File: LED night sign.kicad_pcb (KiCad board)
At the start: 2 copper layers, 42.9 x 36.7 mm, 38 parts, among them Q1 MOSFET-NCH-2N7002PW, Q2 BC817, U1 ATtiny85-20M, U2 APDS-9301

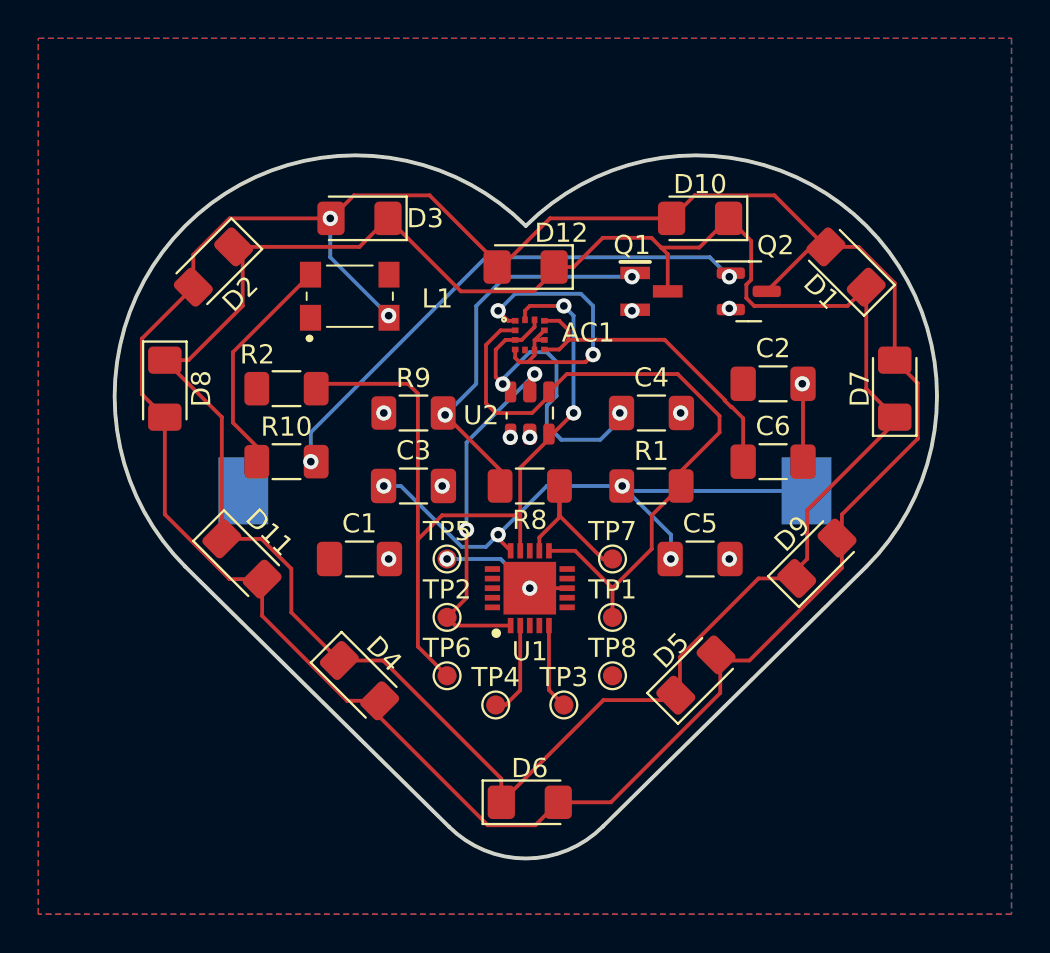
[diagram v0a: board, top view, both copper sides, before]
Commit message: Enh pcb layout
repositioned leds to be more symmetrical
improved silkscreens
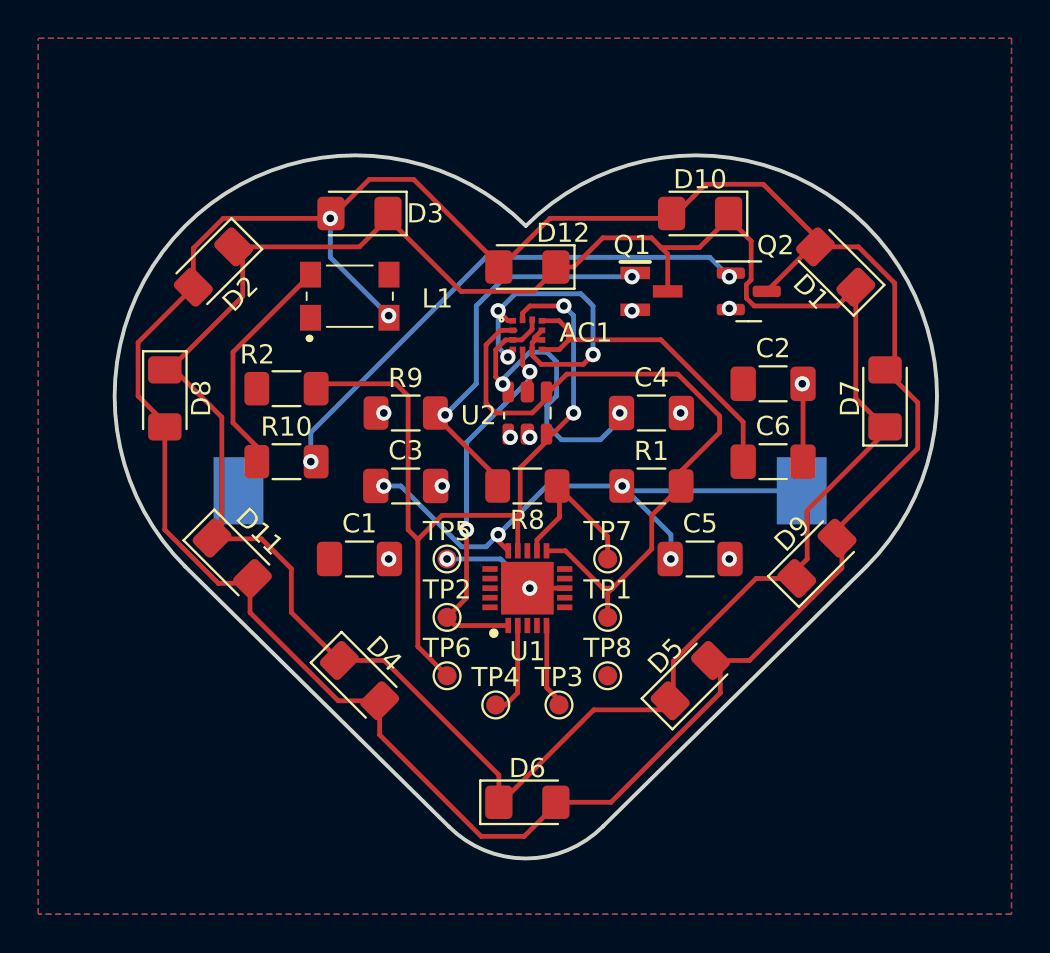
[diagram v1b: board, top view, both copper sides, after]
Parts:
- BT1: value Battery_Cell -> 2032
- moved D7 0.72 mm to (168.7, 98.6)
- moved D1 0.54 mm to (166.1, 91.7)
- moved D11 0.51 mm to (134.6, 106.9)
- moved D8 0.51 mm to (131.1, 98.6)
- moved D5 0.41 mm to (158.5, 113.3)
- moved C3 0.41 mm to (143.6, 103.1)
- moved R9 0.41 mm to (143.6, 99.3)
- moved BT1 0.25 mm to (149.6, 103.4)
- moved D10 0.25 mm to (159.0, 88.9)
- moved D3 0.25 mm to (141.2, 88.9)
- moved TP1 0.25 mm to (154.2, 110.0)
- moved TP3 0.25 mm to (151.6, 114.6)
- moved TP7 0.25 mm to (154.2, 106.9)
- moved TP8 0.25 mm to (154.2, 113.0)
- moved AC1 0.13 mm to (150.0, 95.2)
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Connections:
- AC1 pad 5: unconnected-(AC1-Pad5) -> INT
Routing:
- net JouleThiefPWR: track 135.7 -> 138.5 mm
- net INT: track 19.1 -> 20.3 mm
- net GND: track 27.5 -> 28.7 mm, vias 14 -> 15

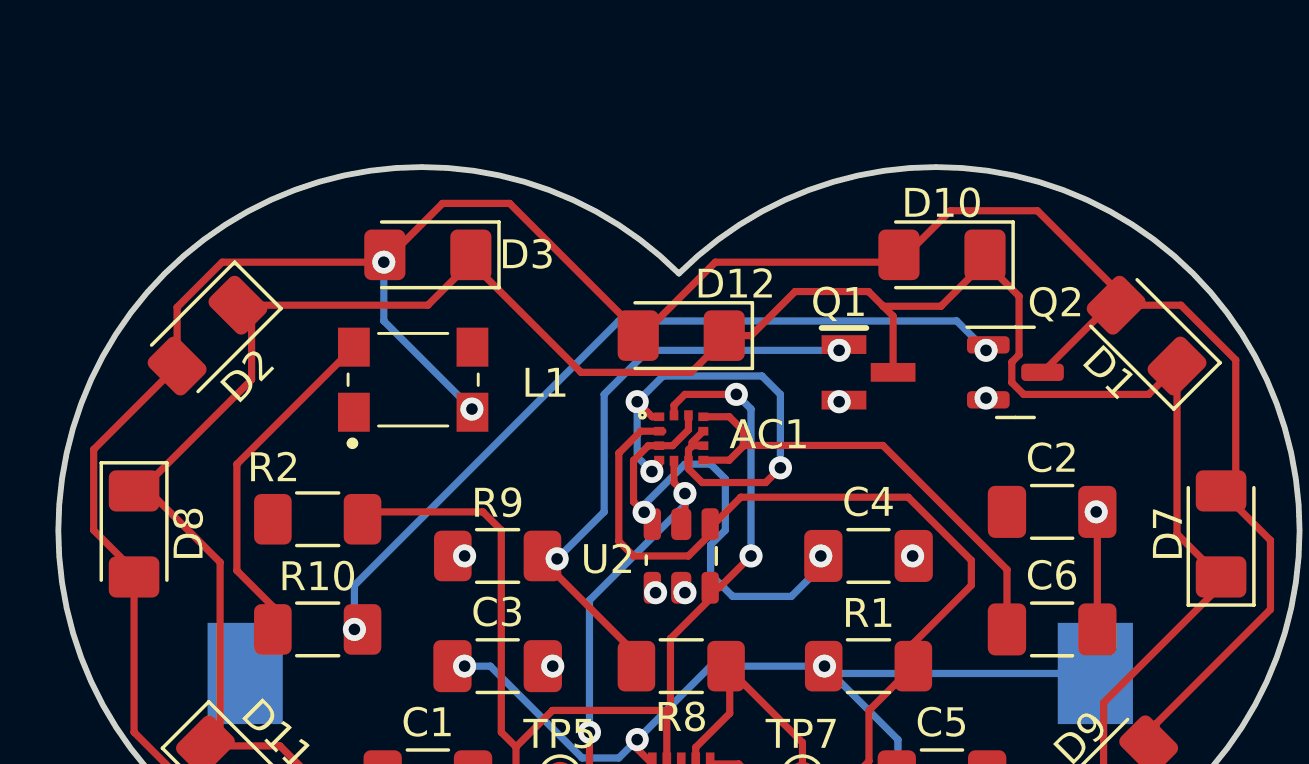
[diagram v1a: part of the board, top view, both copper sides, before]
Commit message: made room for potential holes
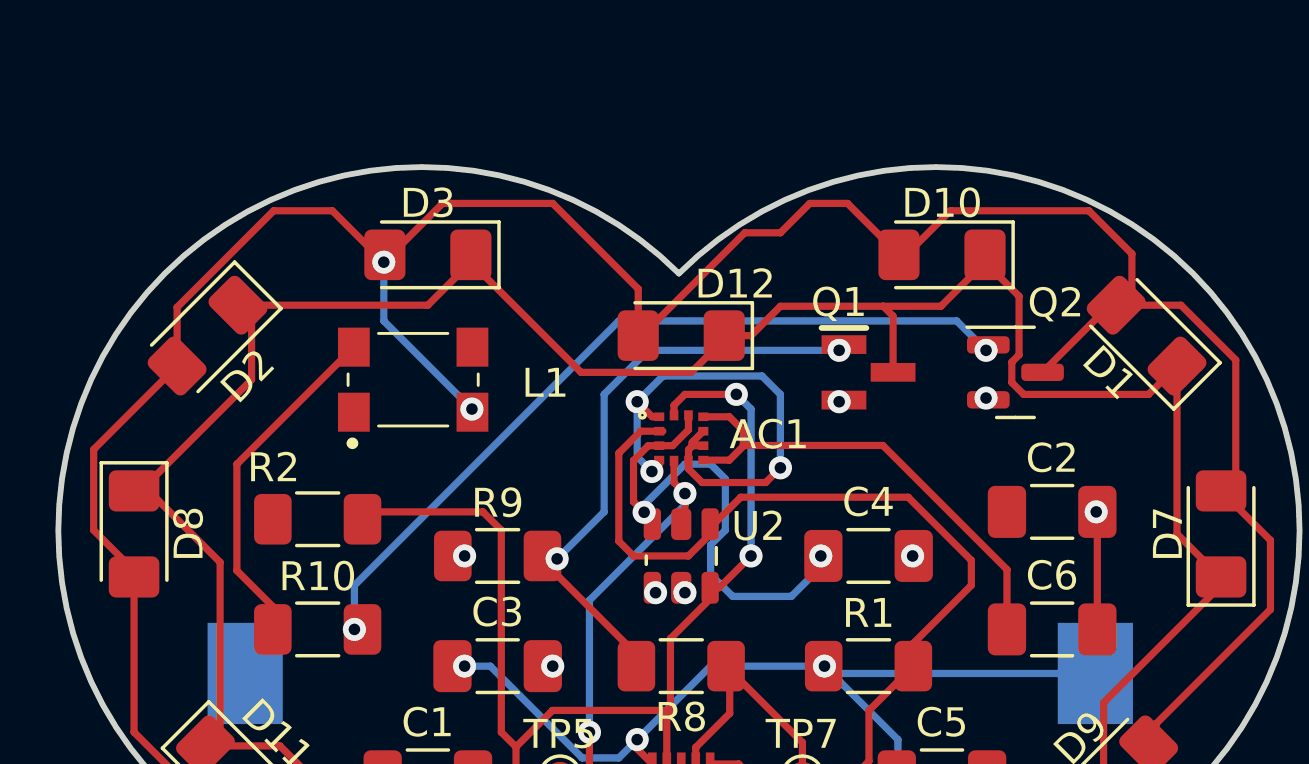
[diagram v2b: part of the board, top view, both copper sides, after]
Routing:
- net JouleThiefPWR: track 138.5 -> 143.2 mm

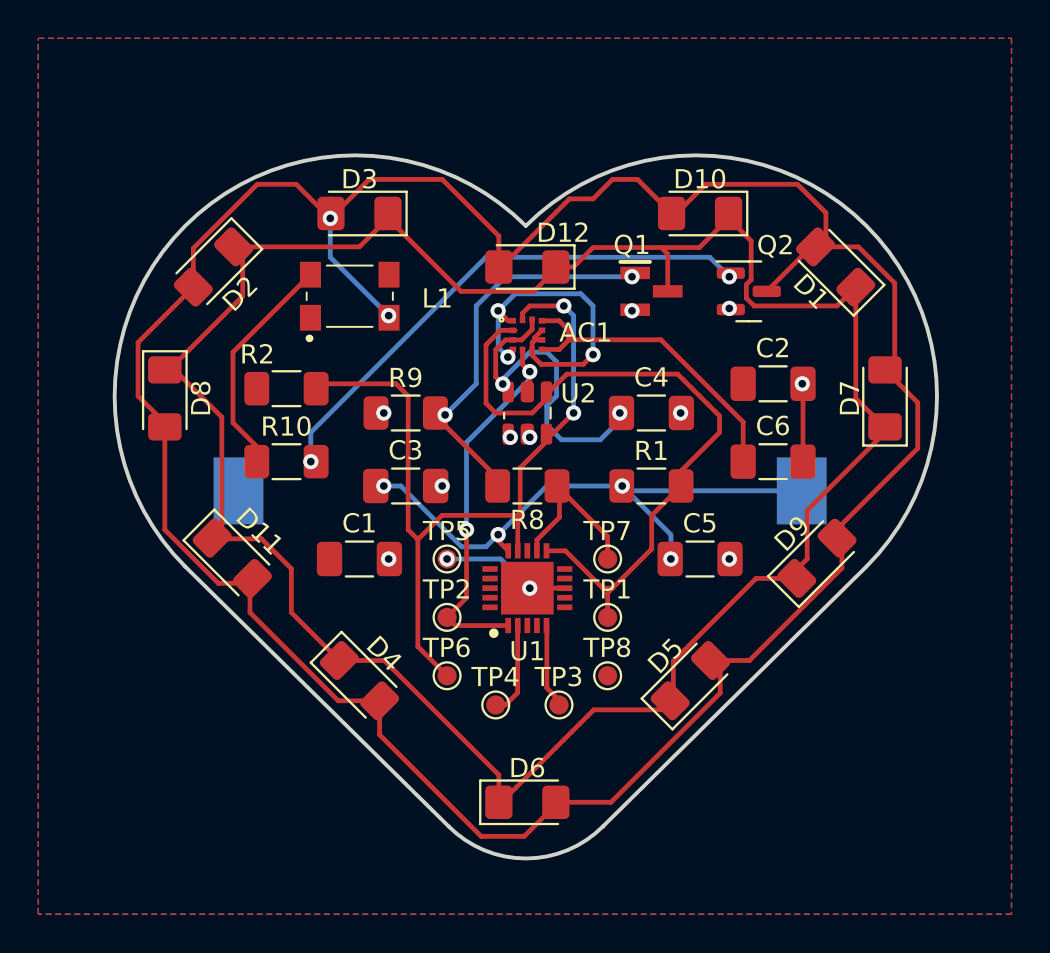
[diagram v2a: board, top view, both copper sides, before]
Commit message: melted the circuit (rounded tracks)
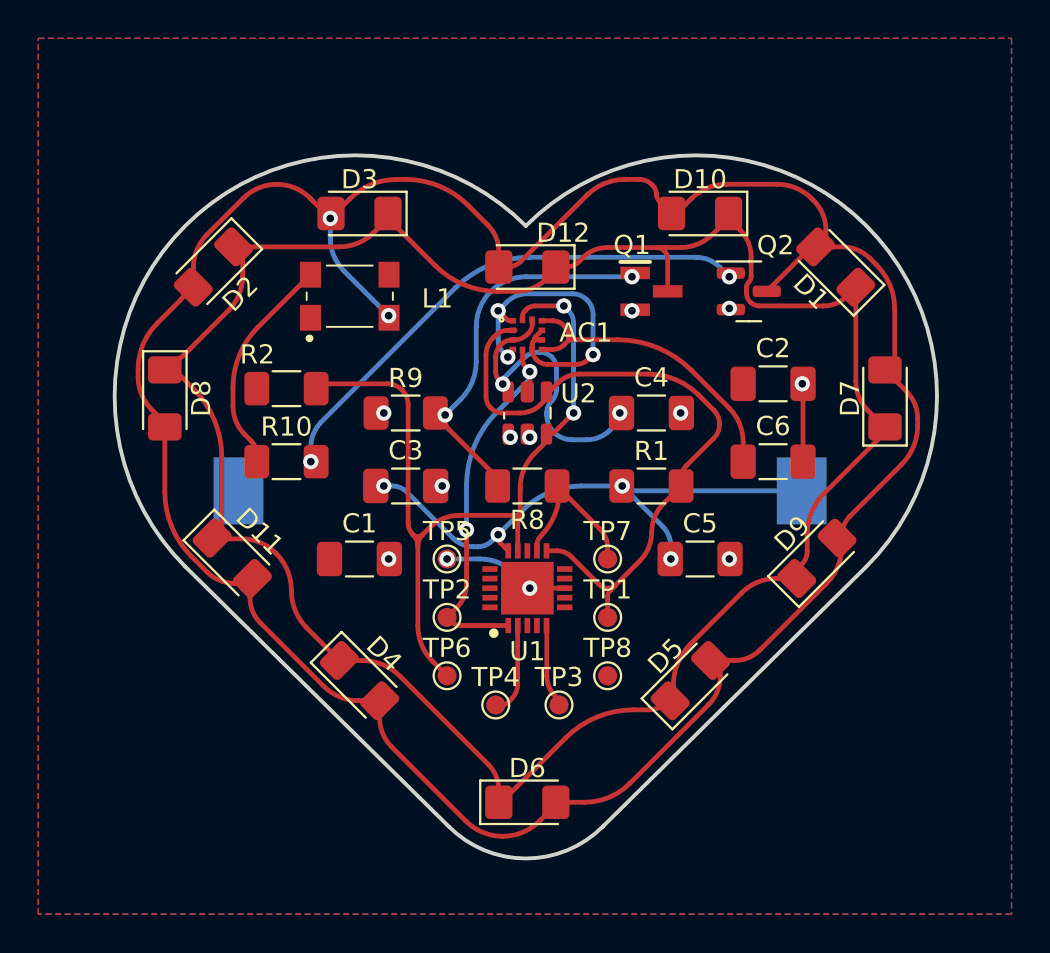
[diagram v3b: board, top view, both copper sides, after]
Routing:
- net Net-(D1-Pad1): track 124.9 -> 118.7 mm
- net JouleThiefPWR: track 143.2 -> 139.3 mm
- net +3V0: track 48.4 -> 47.2 mm
- net PB0/SDA/MOSI: track 36.2 -> 35.5 mm
- net CTRLLED: track 8.83 -> 8.17 mm
- net INT: track 20.3 -> 19.8 mm

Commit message: enh pcb and sch
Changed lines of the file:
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@@
   (segment (start 134.6835 108.204) (end 134.747 108.204) (width 0.25) (layer "F.Cu") (net 4))
   (segment (start 151.6015 119.634) (end 152.976278 119.634) (width 0.25) (layer "F.Cu") (net 4))
-  (segment (start 148.4995 91.6305) (end 148.4995 90.88675) (width 0.25) (layer "F.Cu") (net 4))
-  (segment (start 166.809932 104.716067) (end 169.519184 102.006815) (width 0.25) (layer "F.Cu") (net 4))
+  (segment (start 148.4995 90.88675) (end 148.4995 91.6305) (width 0.25) (layer "F.Cu") (net 4))
+  (segment (start 169.519184 102.006815) (end 166.809932 104.716067) (width 0.25) (layer "F.Cu") (net 4))
   (segment (start 156.551299 87.463299) (end 156.464 87.376) (width 0.25) (layer "F.Cu") (net 4))
   (segment (start 169.764 98.1725) (end 169.164 97.5725) (width 0.25) (layer "F.Cu") (net 4))
@@
   (segment (start 139.353499 113.572499) (end 136.047815 110.266815) (width 0.25) (layer "F.Cu") (net 4))
   (segment (start 141.196321 114.335821) (end 141.386821 114.335821) (width 0.25) (layer "F.Cu") (net 4))
-  (segment (start 160.436821 112.232179) (end 160.817821 112.232179) (width 0.25) (layer "F.Cu") (net 4))
-  (segment (start 142.904438 116.742438) (end 146.778681 120.616681) (width 0.25) (layer "F.Cu") (net 4))
+  (segment (start 160.817821 112.232179) (end 160.436821 112.232179) (width 0.25) (layer "F.Cu") (net 4))
+  (segment (start 146.778681 120.616681) (end 142.904438 116.742438) (width 0.25) (layer "F.Cu") (net 4))
   (segment (start 158.5325 88.138) (end 157.7705 88.9) (width 0.25) (layer "F.Cu") (net 4))
   (segment (start 156.8847 88.2682) (end 157.5165 88.9) (width 0.25) (layer "F.Cu") (net 4))
@@
   (arc (start 140.716 88.138) (mid 141.841372 87.386049) (end 143.16884 87.122) (width 0.25) (layer "F.Cu") (net 4))
   (arc (start 129.667 97.437171) (mid 129.848534 98.349805) (end 130.3655 99.1235) (width 0.25) (layer "F.Cu") (net 4))
-  (arc (start 156.464 87.376) (mid 156.182656 87.188012) (end 155.850789 87.122) (width 0.25) (layer "F.Cu") (net 4))
-  (arc (start 142.904438 116.742438) (mid 142.439193 116.046149) (end 142.275821 115.224821) (width 0.25) (layer "F.Cu") (net 4))
-  (arc (start 149.653404 91.392595) (mid 149.319553 91.615667) (end 148.92575 91.694) (width 0.25) (layer "F.Cu") (net 4))
+  (arc (start 155.850789 87.122) (mid 156.182656 87.188012) (end 156.464 87.376) (width 0.25) (layer "F.Cu") (net 4))
+  (arc (start 142.275821 115.224821) (mid 142.439193 116.046149) (end 142.904438 116.742438) (width 0.25) (layer "F.Cu") (net 4))
+  (arc (start 148.92575 91.694) (mid 149.319553 91.615667) (end 149.653404 91.392595) (width 0.25) (layer "F.Cu") (net 4))
   (arc (start 156.551299 87.463299) (mid 156.674675 87.647945) (end 156.718 87.86575) (width 0.25) (layer "F.Cu") (net 4))
   (arc (start 132.461 106.807) (mid 131.427068 105.259611) (end 131.064 103.434343) (width 0.25) (layer "F.Cu") (net 4))
@@
   (arc (start 138.64042 88.09442) (mid 137.844661 87.562711) (end 136.906 87.376) (width 0.25) (layer "F.Cu") (net 4))
   (arc (start 132.552179 91.729821) (mid 132.365467 92.668482) (end 131.833758 93.464241) (width 0.25) (layer "F.Cu") (net 4))
-  (arc (start 156.718 87.86575) (mid 156.761323 88.083554) (end 156.8847 88.2682) (width 0.25) (layer "F.Cu") (net 4))
+  (arc (start 156.8847 88.2682) (mid 156.761323 88.083554) (end 156.718 87.86575) (width 0.25) (layer "F.Cu") (net 4))
   (arc (start 160.055821 113.080707) (mid 159.899886 113.864644) (end 159.455821 114.529234) (width 0.25) (layer "F.Cu") (net 4))
   (arc (start 166.405821 106.263179) (mid 166.19577 107.319173) (end 165.597597 108.214402) (width 0.25) (layer "F.Cu") (net 4))
@@
   (arc (start 168.216617 91.589561) (mid 168.917783 92.63893) (end 169.164 93.876745) (width 0.25) (layer "F.Cu") (net 4))
   (arc (start 146.889038 88.469038) (mid 145.39699 87.472083) (end 143.637 87.122) (width 0.25) (layer "F.Cu") (net 4))
-  (arc (start 160.436821 112.232179) (mid 160.167413 112.343771) (end 160.055821 112.613179) (width 0.25) (layer "F.Cu") (net 4))
+  (arc (start 160.055821 112.613179) (mid 160.167413 112.343771) (end 160.436821 112.232179) (width 0.25) (layer "F.Cu") (net 4))
   (segment (start 139.7 89.154) (end 139.7 90.17) (width 0.25) (layer "B.Cu") (net 4))
   (segment (start 140.41842 91.90442) (end 142.748 94.234) (width 0.25) (layer "B.Cu") (net 4))
